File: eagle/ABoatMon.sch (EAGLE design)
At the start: 26 parts, among them J1 5V, J2 GND, J3 GND, J4 5V

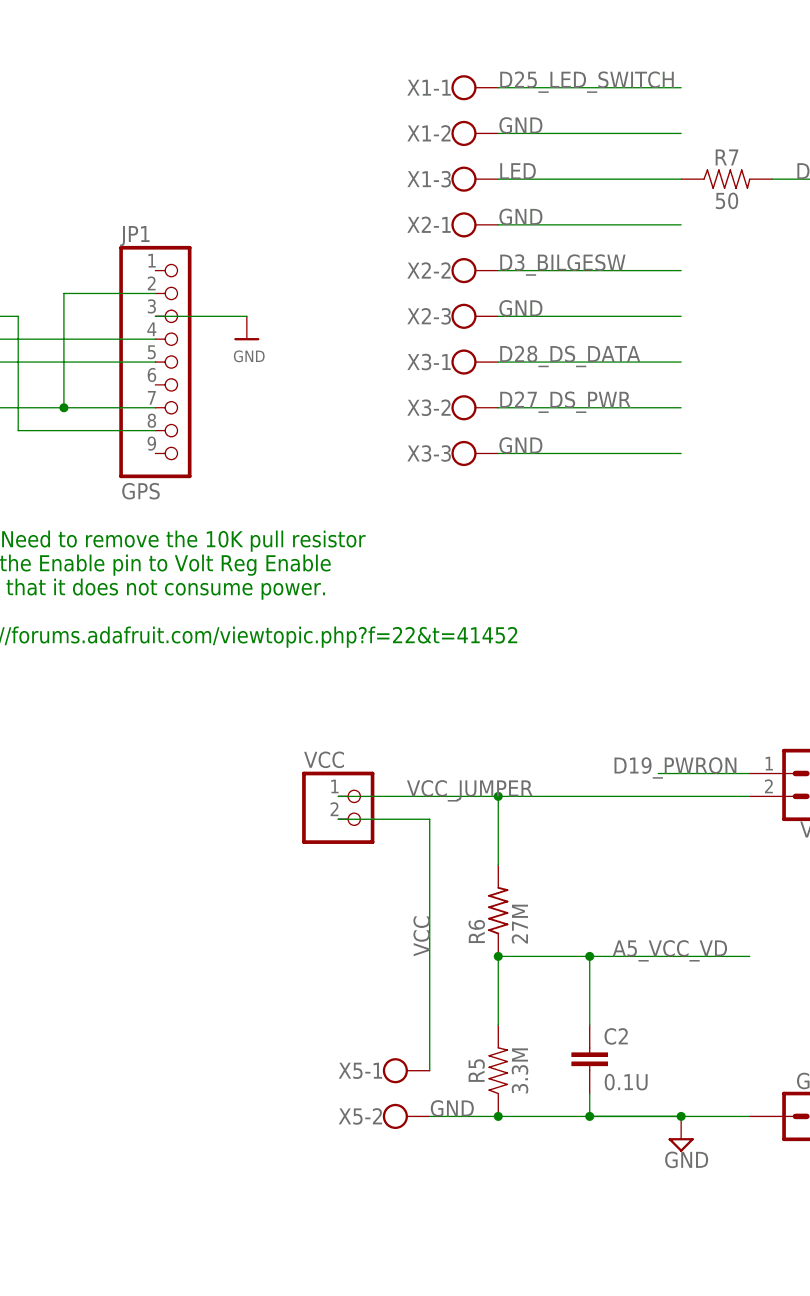
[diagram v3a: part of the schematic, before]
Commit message: v0.649 - moved screw terminal headers
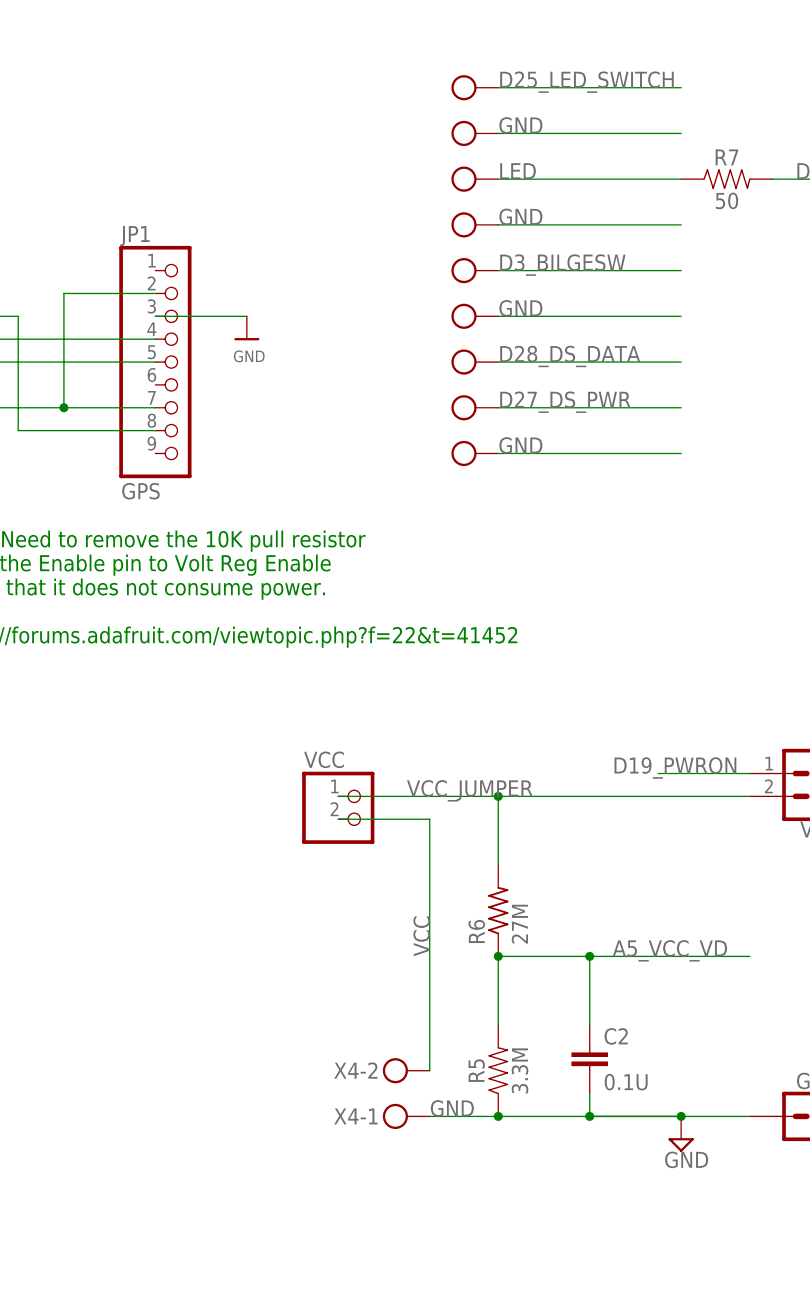
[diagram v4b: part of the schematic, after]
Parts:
- removed X2, X3: (no value), con-wago-500:W237-103
- added X4: MKDSN1,5/2-5,08, con-phoenix-508:MKDSN1,5/2-5,08
- added X6: MKDSN1,5/3-5,08, con-phoenix-508:MKDSN1,5/3-5,08
- X1: value (none) -> MKDSN1,5/3-5,08; device con-wago-500:W237-103 -> con-phoenix-508:MKDSN1,5/3-5,08
- X5: value (none) -> MKDSN1,5/3-5,08; device con-wago-500:W237-102 -> con-phoenix-508:MKDSN1,5/3-5,08; SPICEPREFIX (none) -> X
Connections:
- net D25_LED_SWITCH: now also X6-1.KL; no longer X1-1.KL
- net D27_DS_PWR: now also X5-2.KL; no longer X3-2.KL
- net D28_DS_DATA: now also X5-3.KL; no longer X3-1.KL
- net D3_BILGESW: now also X1-2.KL; no longer X2-2.KL
- net GND: now also X1-1.KL, X1-3.KL, X4-1.KL, X5-1.KL, X6-2.KL; no longer X1-2.KL, X2-1.KL, X2-3.KL, X3-3.KL, X5-2.KL
- net LED: now also X6-3.KL; no longer X1-3.KL
- net VCC: now also X4-2.KL; no longer X5-1.KL
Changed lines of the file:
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@@
 <?xml version="1.0" encoding="utf-8"?>
 <!DOCTYPE eagle SYSTEM "eagle.dtd">
-<eagle version="9.2.1">
+<eagle version="9.2.2">
 <drawing>
 <settings>
@@
 <part name="J3" library="SparkFun-Connectors" deviceset="CONN_01" device="" value="GND"/>
 <part name="SUPPLY3" library="supply2" deviceset="GND" device=""/>
-<part name="X1" library="con-wago-500" library_urn="urn:adsk.eagle:library:195" deviceset="W237-103" device="" package3d_urn="urn:adsk.eagle:package:10691/1"/>
-<part name="X2" library="con-wago-500" library_urn="urn:adsk.eagle:library:195" deviceset="W237-103" device="" package3d_urn="urn:adsk.eagle:package:10691/1"/>
-<part name="X3" library="con-wago-500" library_urn="urn:adsk.eagle:library:195" deviceset="W237-103" device="" package3d_urn="urn:adsk.eagle:package:10691/1"/>
 <part name="U$2" library="microbuilder" deviceset="MOUNTINGHOLE" device="2.5"/>
 <part name="U$3" library="microbuilder" deviceset="MOUNTINGHOLE" device="2.5"/>
@@
 <part name="LIPO" library="microbuilder" deviceset="HEADER-1X2" device="ROUND"/>
 <part name="J4" library="SparkFun-Connectors" deviceset="CONN_01" device="" value="5V"/>
-<part name="X5" library="con-wago-500" library_urn="urn:adsk.eagle:library:195" deviceset="W237-102" device="" package3d_urn="urn:adsk.eagle:package:10688/1"/>
+<part name="X4" library="con-phoenix-508" library_urn="urn:adsk.eagle:library:176" deviceset="MKDSN1,5/2-5,08" device="" package3d_urn="urn:adsk.eagle:package:9630/1"/>
+<part name="X6" library="con-phoenix-508" library_urn="urn:adsk.eagle:library:176" deviceset="MKDSN1,5/3-5,08" device="" package3d_urn="urn:adsk.eagle:package:9641/1"/>
+<part name="X1" library="con-phoenix-508" library_urn="urn:adsk.eagle:library:176" deviceset="MKDSN1,5/3-5,08" device="" package3d_urn="urn:adsk.eagle:package:9641/1"/>
+<part name="X5" library="con-phoenix-508" library_urn="urn:adsk.eagle:library:176" deviceset="MKDSN1,5/3-5,08" device="" package3d_urn="urn:adsk.eagle:package:9641/1">
+<attribute name="SPICEPREFIX" value="X"/>
+</part>
 </parts>
 <sheets>
@@
 <attribute name="VALUE" x="56.515" y="108.585" size="1.778" layer="96"/>
 </instance>
-<instance part="X1" gate="-1" x="182.88" y="160.02" smashed="yes">
-<attribute name="NAME" x="182.88" y="160.909" size="1.778" layer="95" rot="R180"/>
-</instance>
-<instance part="X1" gate="-2" x="182.88" y="154.94" smashed="yes">
-<attribute name="NAME" x="182.88" y="155.829" size="1.778" layer="95" rot="R180"/>
-</instance>
-<instance part="X1" gate="-3" x="182.88" y="149.86" smashed="yes">
-<attribute name="VALUE" x="180.34" y="146.177" size="1.778" layer="96"/>
-<attribute name="NAME" x="182.88" y="150.749" size="1.778" layer="95" rot="R180"/>
-</instance>
-<instance part="X2" gate="-1" x="182.88" y="144.78" smashed="yes">
-<attribute name="NAME" x="182.88" y="145.669" size="1.778" layer="95" rot="R180"/>
-</instance>
-<instance part="X2" gate="-2" x="182.88" y="139.7" smashed="yes">
-<attribute name="NAME" x="182.88" y="140.589" size="1.778" layer="95" rot="R180"/>
-</instance>
-<instance part="X2" gate="-3" x="182.88" y="134.62" smashed="yes">
-<attribute name="VALUE" x="180.34" y="130.937" size="1.778" layer="96"/>
-<attribute name="NAME" x="182.88" y="135.509" size="1.778" layer="95" rot="R180"/>
-</instance>
-<instance part="X3" gate="-1" x="182.88" y="129.54" smashed="yes">
-<attribute name="NAME" x="182.88" y="130.429" size="1.778" layer="95" rot="R180"/>
-</instance>
-<instance part="X3" gate="-2" x="182.88" y="124.46" smashed="yes">
-<attribute name="NAME" x="182.88" y="125.349" size="1.778" layer="95" rot="R180"/>
-</instance>
-<instance part="X3" gate="-3" x="182.88" y="119.38" smashed="yes">
-<attribute name="VALUE" x="180.34" y="115.697" size="1.778" layer="96"/>
-<attribute name="NAME" x="182.88" y="120.269" size="1.778" layer="95" rot="R180"/>
-</instance>
 <instance part="U$2" gate="G$1" x="66.04" y="20.32" smashed="yes"/>
 <instance part="U$3" gate="G$1" x="73.66" y="20.32" smashed="yes"/>
@@
 <attribute name="NAME" x="55.88" y="58.928" size="1.778" layer="95" font="vector"/>
 </instance>
-<instance part="X5" gate="-1" x="175.26" y="50.8" smashed="yes">
-<attribute name="NAME" x="175.26" y="51.689" size="1.778" layer="95" rot="R180"/>
-</instance>
-<instance part="X5" gate="-2" x="175.26" y="45.72" smashed="yes">
-<attribute name="VALUE" x="172.72" y="42.037" size="1.778" layer="96"/>
-<attribute name="NAME" x="175.26" y="46.609" size="1.778" layer="95" rot="R180"/>
-</instance>
+<instance part="X4" gate="-1" x="177.8" y="45.72" smashed="yes" rot="R180">
+<attribute name="NAME" x="174.752" y="46.609" size="1.778" layer="95" rot="R180"/>
+</instance>
+<instance part="X4" gate="-2" x="177.8" y="50.8" smashed="yes" rot="R180">
+<attribute name="NAME" x="174.752" y="51.689" size="1.778" layer="95" rot="R180"/>
+</instance>
+<instance part="X6" gate="-1" x="185.42" y="160.02" smashed="yes" rot="R180"/>
+<instance part="X6" gate="-2" x="185.42" y="154.94" smashed="yes" rot="R180"/>
+<instance part="X6" gate="-3" x="185.42" y="149.86" smashed="yes" rot="R180"/>
+<instance part="X1" gate="-1" x="185.42" y="134.62" smashed="yes" rot="R180"/>
+<instance part="X1" gate="-2" x="185.42" y="139.7" smashed="yes" rot="R180"/>
+<instance part="X1" gate="-3" x="185.42" y="144.78" smashed="yes" rot="R180"/>
+<instance part="X5" gate="-1" x="185.42" y="119.38" smashed="yes" rot="R180"/>
+<instance part="X5" gate="-2" x="185.42" y="124.46" smashed="yes" rot="R180"/>
+<instance part="X5" gate="-3" x="185.42" y="129.54" smashed="yes" rot="R180"/>
 </instances>
 <busses>
@@
 <junction x="198.12" y="45.72"/>
 <pinref part="J3" gate="G$1" pin="1"/>
-<pinref part="X5" gate="-2" pin="KL"/>
+<pinref part="X4" gate="-1" pin="KL"/>
 </segment>
 <segment>
@@
 <wire x1="187.96" y1="154.94" x2="208.28" y2="154.94" width="0.1524" layer="91"/>
 <label x="187.96" y="154.94" size="1.778" layer="95"/>
-<pinref part="X1" gate="-2" pin="KL"/>
+<pinref part="X6" gate="-2" pin="KL"/>
 </segment>
 <segment>
 <wire x1="187.96" y1="144.78" x2="208.28" y2="144.78" width="0.1524" layer="91"/>
 <label x="187.96" y="144.78" size="1.778" layer="95"/>
-<pinref part="X2" gate="-1" pin="KL"/>
+<pinref part="X1" gate="-3" pin="KL"/>
 </segment>
 <segment>
 <wire x1="187.96" y1="134.62" x2="208.28" y2="134.62" width="0.1524" layer="91"/>
 <label x="187.96" y="134.62" size="1.778" layer="95"/>
-<pinref part="X2" gate="-3" pin="KL"/>
+<pinref part="X1" gate="-1" pin="KL"/>
 </segment>
 <segment>
 <wire x1="187.96" y1="119.38" x2="208.28" y2="119.38" width="0.1524" layer="91"/>
 <label x="187.96" y="119.38" size="1.778" layer="95"/>
-<pinref part="X3" gate="-3" pin="KL"/>
+<pinref part="X5" gate="-1" pin="KL"/>
 </segment>
 <segment>
@@
 <pinref part="VCC" gate="G$1" pin="2"/>
 <wire x1="170.18" y1="78.74" x2="180.34" y2="78.74" width="0.1524" layer="91"/>
-<pinref part="X5" gate="-1" pin="KL"/>
+<pinref part="X4" gate="-2" pin="KL"/>
 </segment>
 </net>
@@
 <pinref part="R7" gate="G$1" pin="1"/>
 <label x="187.96" y="149.86" size="1.778" layer="95"/>
-<pinref part="X1" gate="-3" pin="KL"/>
+<pinref part="X6" gate="-3" pin="KL"/>
 </segment>
 </net>
@@
 <wire x1="187.96" y1="160.02" x2="208.28" y2="160.02" width="0.1524" layer="91"/>
 <label x="187.96" y="160.02" size="1.778" layer="95"/>
-<pinref part="X1" gate="-1" pin="KL"/>
+<pinref part="X6" gate="-1" pin="KL"/>
 </segment>
 <segment>
@@
 <wire x1="187.96" y1="139.7" x2="208.28" y2="139.7" width="0.1524" layer="91"/>
 <label x="187.96" y="139.7" size="1.778" layer="95"/>
-<pinref part="X2" gate="-2" pin="KL"/>
+<pinref part="X1" gate="-2" pin="KL"/>
 </segment>
 <segment>
@@
 <wire x1="187.96" y1="129.54" x2="208.28" y2="129.54" width="0.1524" layer="91"/>
 <label x="187.96" y="129.54" size="1.778" layer="95"/>
-<pinref part="X3" gate="-1" pin="KL"/>
+<pinref part="X5" gate="-3" pin="KL"/>
 </segment>
 <segment>
@@
 <wire x1="187.96" y1="124.46" x2="208.28" y2="124.46" width="0.1524" layer="91"/>
 <label x="187.96" y="124.46" size="1.778" layer="95"/>
-<pinref part="X3" gate="-2" pin="KL"/>
-</segment>
-</net>
+<pinref part="X5" gate="-2" pin="KL"/>
+</segment>
+</net>
